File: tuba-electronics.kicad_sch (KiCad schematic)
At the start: 22 parts, among them J1 Conn_01x08, J10 Conn_01x06, J11 Conn_01x04, J12 Conn_01x04, J13 Conn_01x04, J2 Conn_01x04, J3 Conn_01x03, J4 Conn_01x08, J5 Qwiic_Connector, J6 Qwiic_Connector, J7 Conn_01x05, J8 Conn_01x10, J9 Conn_01x05, U1 MP1584, U3 ESP32-DevKitC

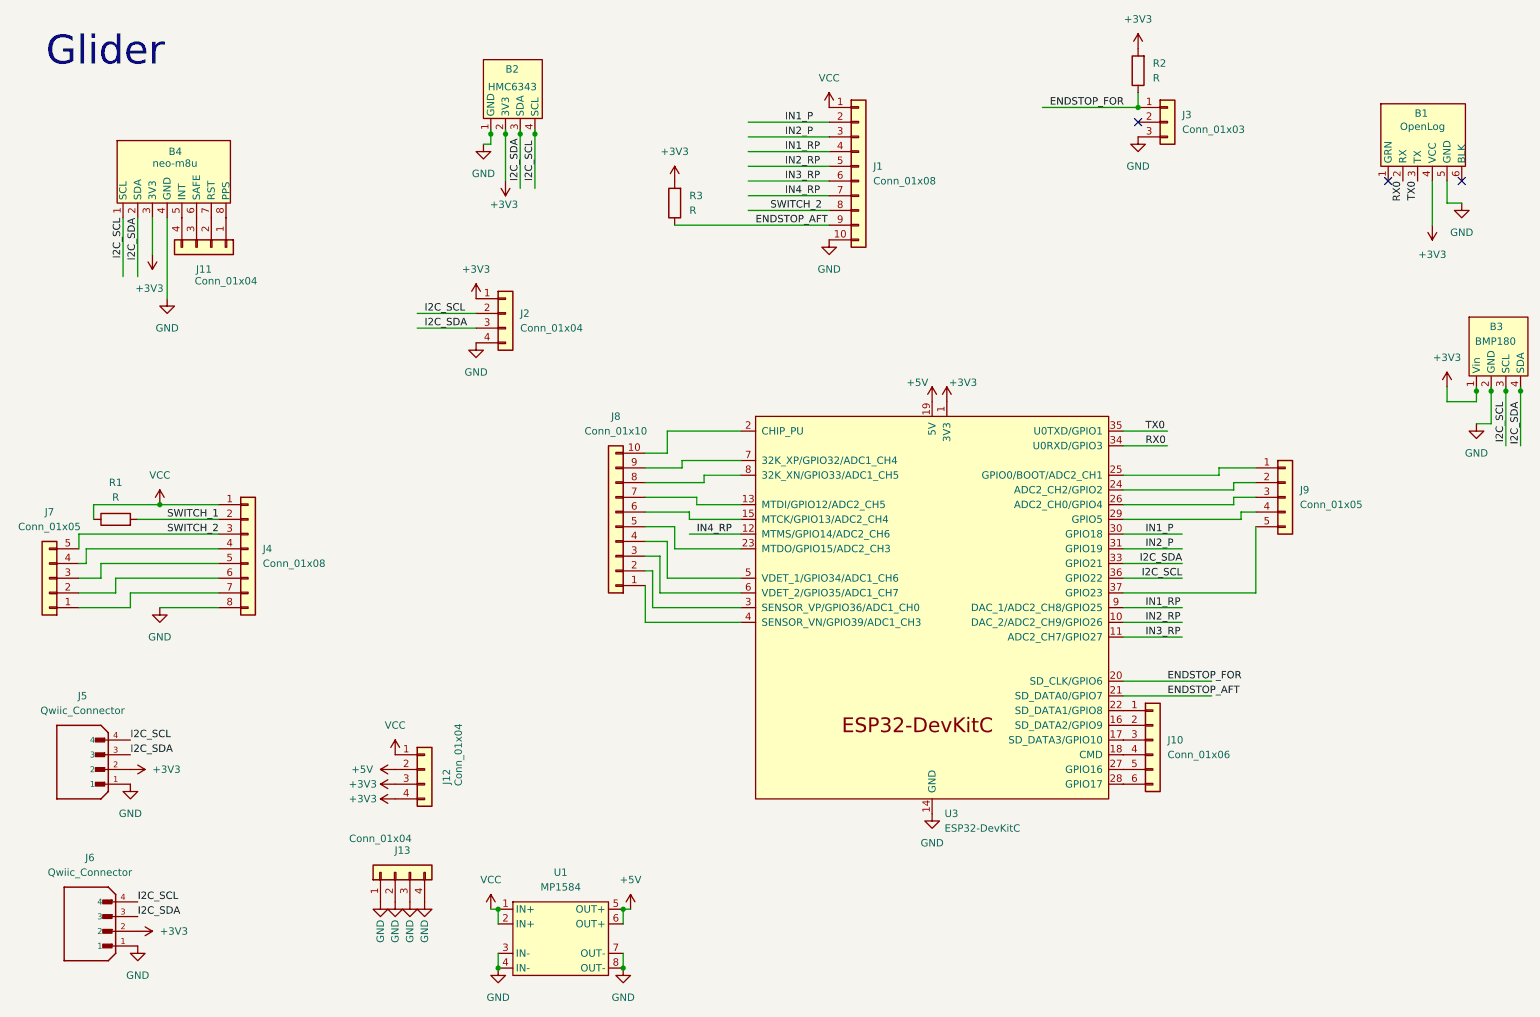
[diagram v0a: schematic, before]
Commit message: changed limit switches GPIOs, added pics
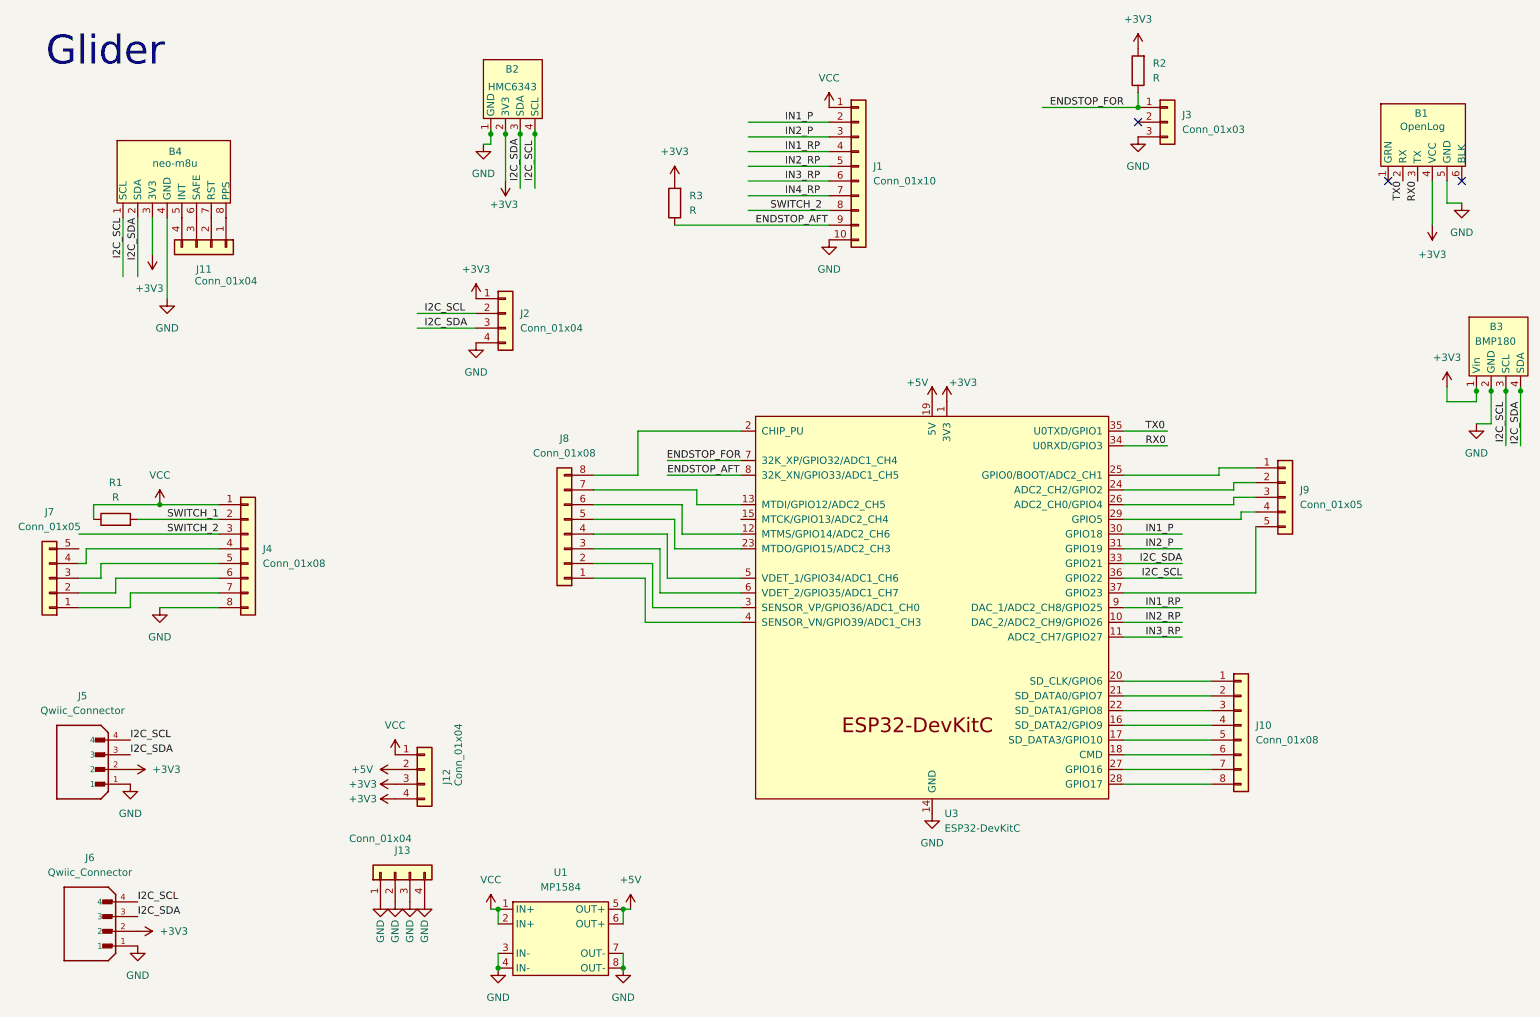
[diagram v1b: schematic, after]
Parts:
- removed J10: Conn_01x06, Connector_PinHeader_2.54mm:PinHeader_1x06_P2.54mm_Vertical, symbol Connector_Generic:Conn_01x06
- removed J8: Conn_01x10, Connector_PinHeader_2.54mm:PinHeader_1x10_P2.54mm_Vertical, symbol Connector_Generic:Conn_01x10
- added J10, J8: Conn_01x08, symbol Connector_Generic:Conn_01x08
- J1: value Conn_01x08 -> Conn_01x10
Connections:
- net ENDSTOP_AFT: now also U3.8 (32K_XN/GPIO33/ADC1_CH5); no longer U3.21 (SD_DATA0/GPIO7)
- net ENDSTOP_FOR: now also U3.7 (32K_XP/GPIO32/ADC1_CH4); no longer U3.20 (SD_CLK/GPIO6)
- net IN4_RP: no longer U3.12 (MTMS/GPIO14/ADC2_CH6)
- net RX0: now also B1.3 (TX); no longer B1.2 (RX)
- net SWITCH_2: no longer J7.5 (Pin_5)
- net TX0: now also B1.2 (RX); no longer B1.3 (TX)
- net at U3.13 (MTDI/GPIO12/ADC2_CH5): now also J8.7 (Pin_7)
- net at U3.16 (SD_DATA2/GPIO9): now also J10.4 (Pin_4)
- net at U3.17 (SD_DATA3/GPIO10): now also J10.5 (Pin_5)
- net at U3.18 (CMD): now also J10.6 (Pin_6)
- net at U3.2 (CHIP_PU): now also J8.8 (Pin_8)
- net at U3.22 (SD_DATA1/GPIO8): now also J10.3 (Pin_3)
- net at U3.23 (MTDO/GPIO15/ADC2_CH3): now also J8.5 (Pin_5)
- net at U3.27 (GPIO16): now also J10.7 (Pin_7)
- net at U3.28 (GPIO17): now also J10.8 (Pin_8)
- net at U3.3 (SENSOR_VP/GPIO36/ADC1_CH0): now also J8.2 (Pin_2)
- net at U3.4 (SENSOR_VN/GPIO39/ADC1_CH3): now also J8.1 (Pin_1)
- net at U3.5 (VDET_1/GPIO34/ADC1_CH6): now also J8.4 (Pin_4)
- net at U3.6 (VDET_2/GPIO35/ADC1_CH7): now also J8.3 (Pin_3)
- new net: J10.1 (Pin_1), U3.20 (SD_CLK/GPIO6)
- new net: J10.2 (Pin_2), U3.21 (SD_DATA0/GPIO7)
- new net: J8.6 (Pin_6), U3.12 (MTMS/GPIO14/ADC2_CH6)

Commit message: adding BOM
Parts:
- R1: value R -> 1k
- R2, R3: value R -> 4k7
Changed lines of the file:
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@@
 			)
 		)
-		(property "Value" "R"
+		(property "Value" "4k7"
 			(at 213.36 26.6699 0)
 			(effects
@@
 			)
 		)
-		(property "Value" "R"
+		(property "Value" "1k"
 			(at 34.29 99.06 90)
 			(effects
@@
 			)
 		)
-		(property "Value" "R"
+		(property "Value" "4k7"
 			(at 133.35 49.5299 0)
 			(effects
